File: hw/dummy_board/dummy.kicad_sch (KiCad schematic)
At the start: 11 parts, among them J1 Conn_02x04, J2 FFC, U1 W25Q128JVS, U2 W25Q128JVS, U3 W25Q128JVP, U4 W25Q128JVS

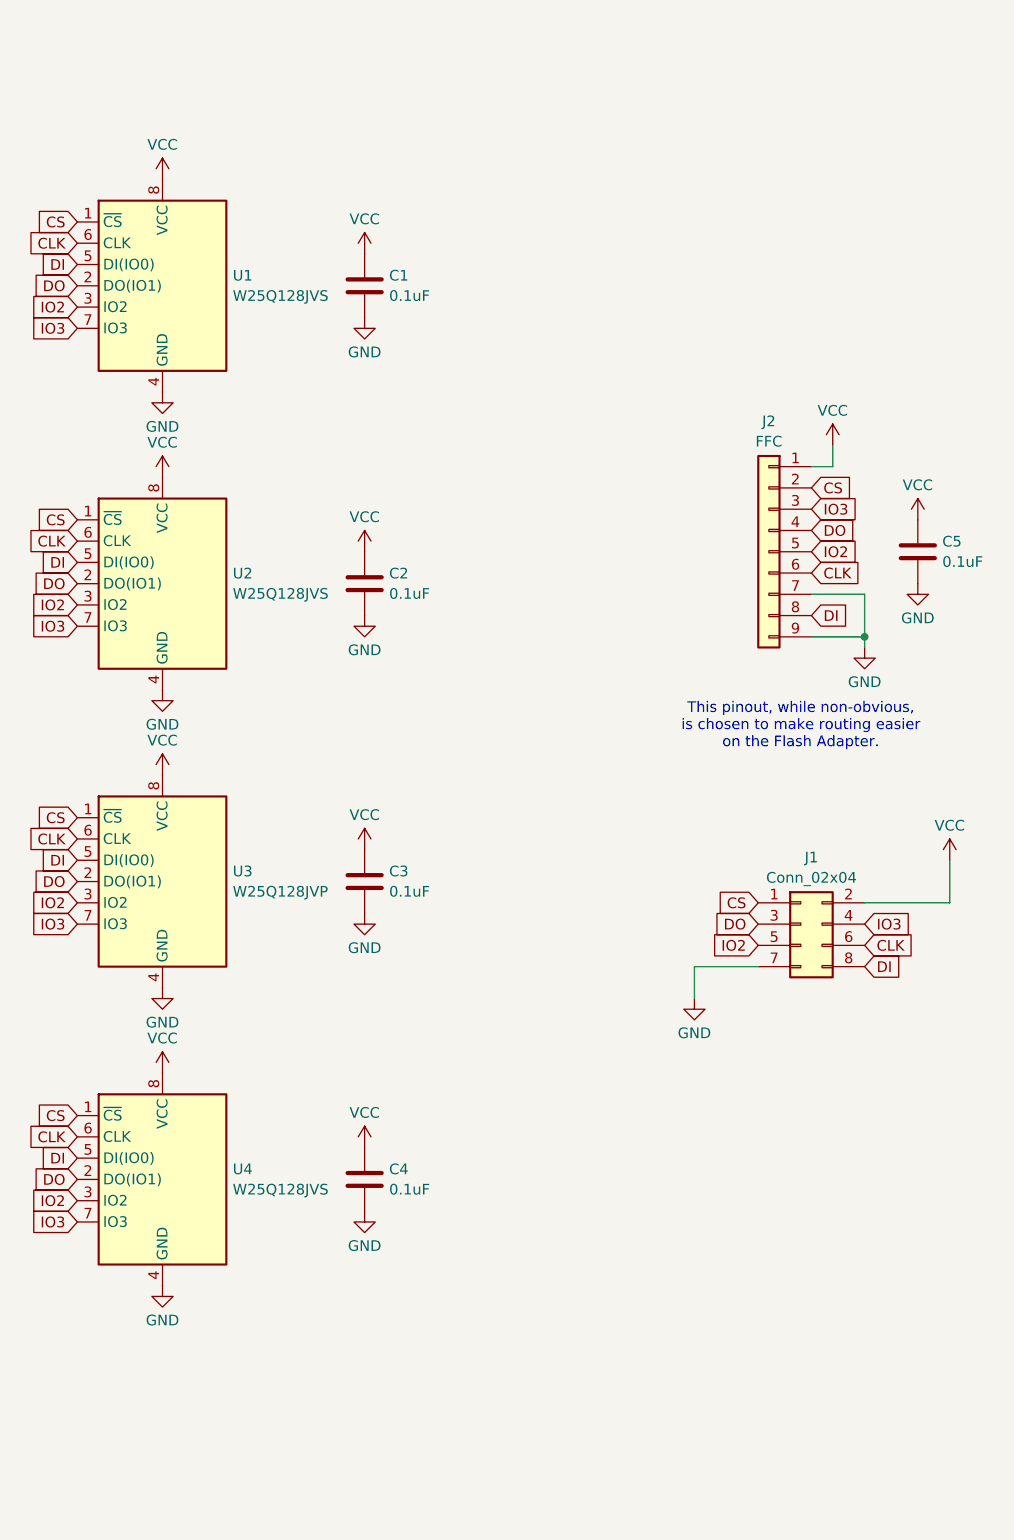
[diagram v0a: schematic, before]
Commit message: Add KiCAD source for Flashkeeper FPGA SoM and its production panel and its associated component libraries. Add basic 3D models for some of the chip packages used. Minimal initial PicoSoC/PicoRV32 configuration and firmware for FPGA SoM bringup. Update gitignores.
Signed-off-by: Dodoid <git-noreply@dodoid.com>
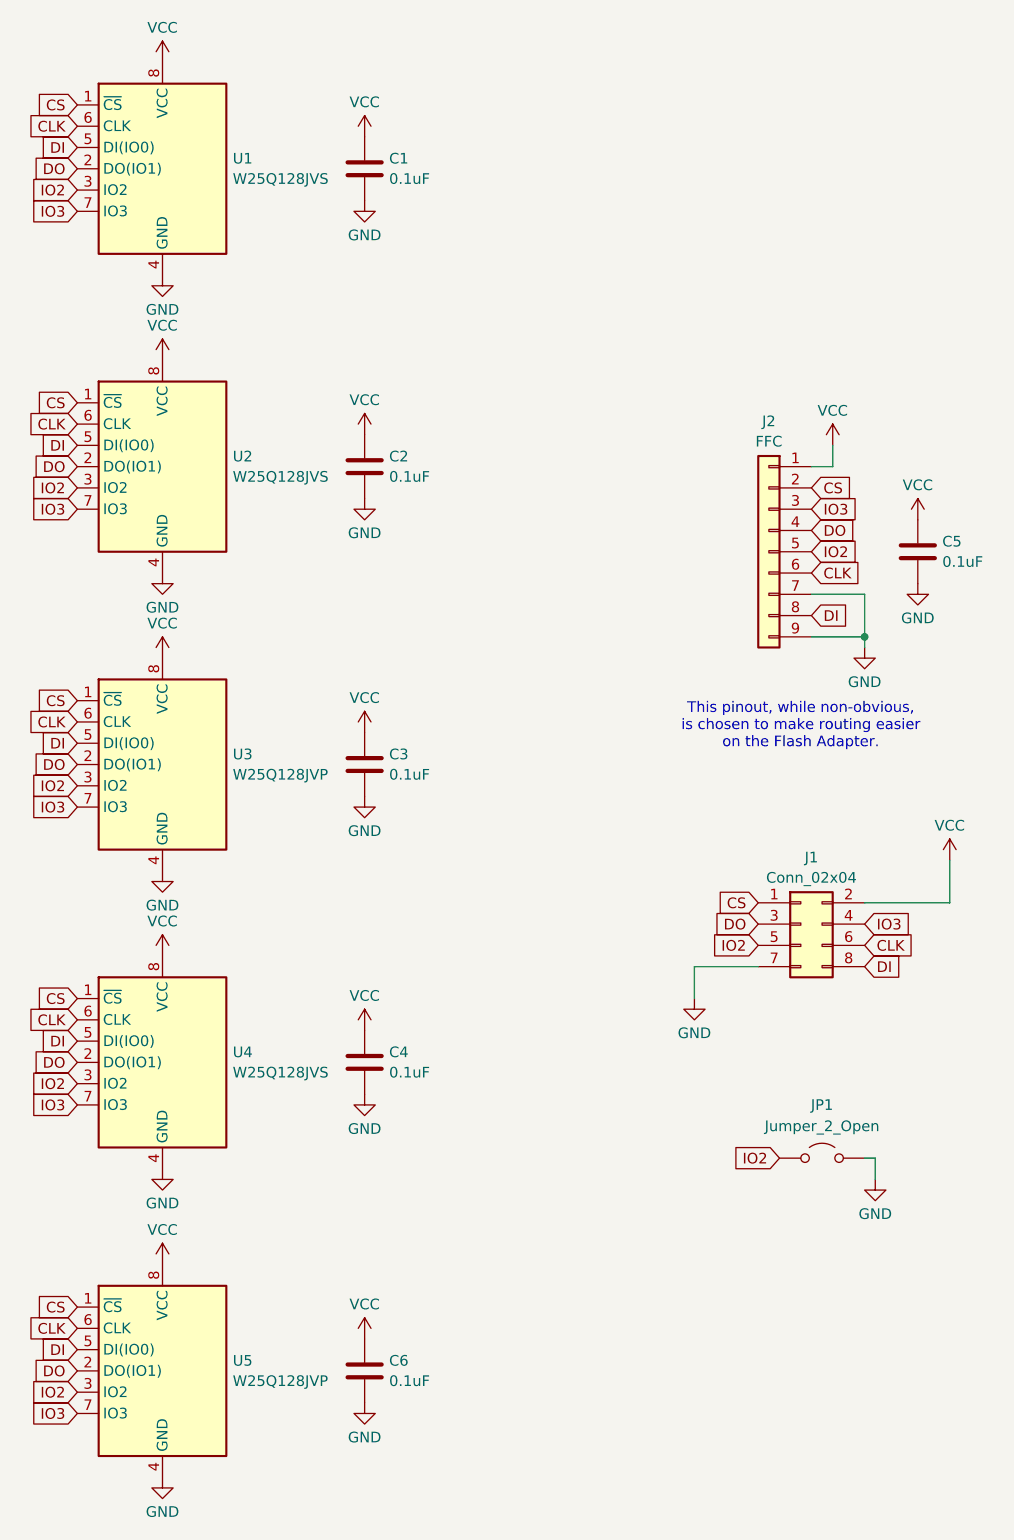
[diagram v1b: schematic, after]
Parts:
- added C6: 0.1uF, Capacitor_SMD:C_0805_2012Metric, symbol Device:C
- added JP1: Jumper_2_Open, Connector_PinHeader_2.54mm:PinHeader_1x02_P2.54mm_Vertical, symbol Jumper:Jumper_2_Open
- added U5: W25Q128JVP, Package_SON:WSON-8-1EP_8x6mm_P1.27mm_EP3.4x4.3mm, symbol Memory_Flash:W25Q128JVP
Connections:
- net CLK: now also U5.6 (CLK)
- net CS: now also U5.1 (~{CS})
- net DI: now also U5.5 (DI(IO0))
- net DO: now also U5.2 (DO(IO1))
- net GND: now also C6.2, JP1.2 (B), U5.4 (GND), U5.9 (GND)
- net IO2: now also JP1.1 (A), U5.3 (IO2)
- net IO3: now also U5.7 (IO3)
- net VCC: now also C6.1, U5.8 (VCC)
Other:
- moved on the sheet: C1, C2, C3, C4, U1, U2, U3, U4
